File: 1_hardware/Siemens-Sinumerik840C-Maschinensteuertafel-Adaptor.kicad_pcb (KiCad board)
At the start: 2 copper layers, 235 x 118.7 mm, 33 parts, among them J111 SSW-132-24-L-D, J121 SSW-132-24-L-D, U1 STM32F103C8T6, U10 PCA9555PW,118, U11 PCA9555PW,118, U2 AP22652AW6-7, U3 LD1117S33CTR, U4 PCA9555PW,118, U5 PCA9555PW,118, U6 PCA9555PW,118, U7 PCA9555PW,118, U8 PCA9555PW,118, U9 PCA9555PW,118

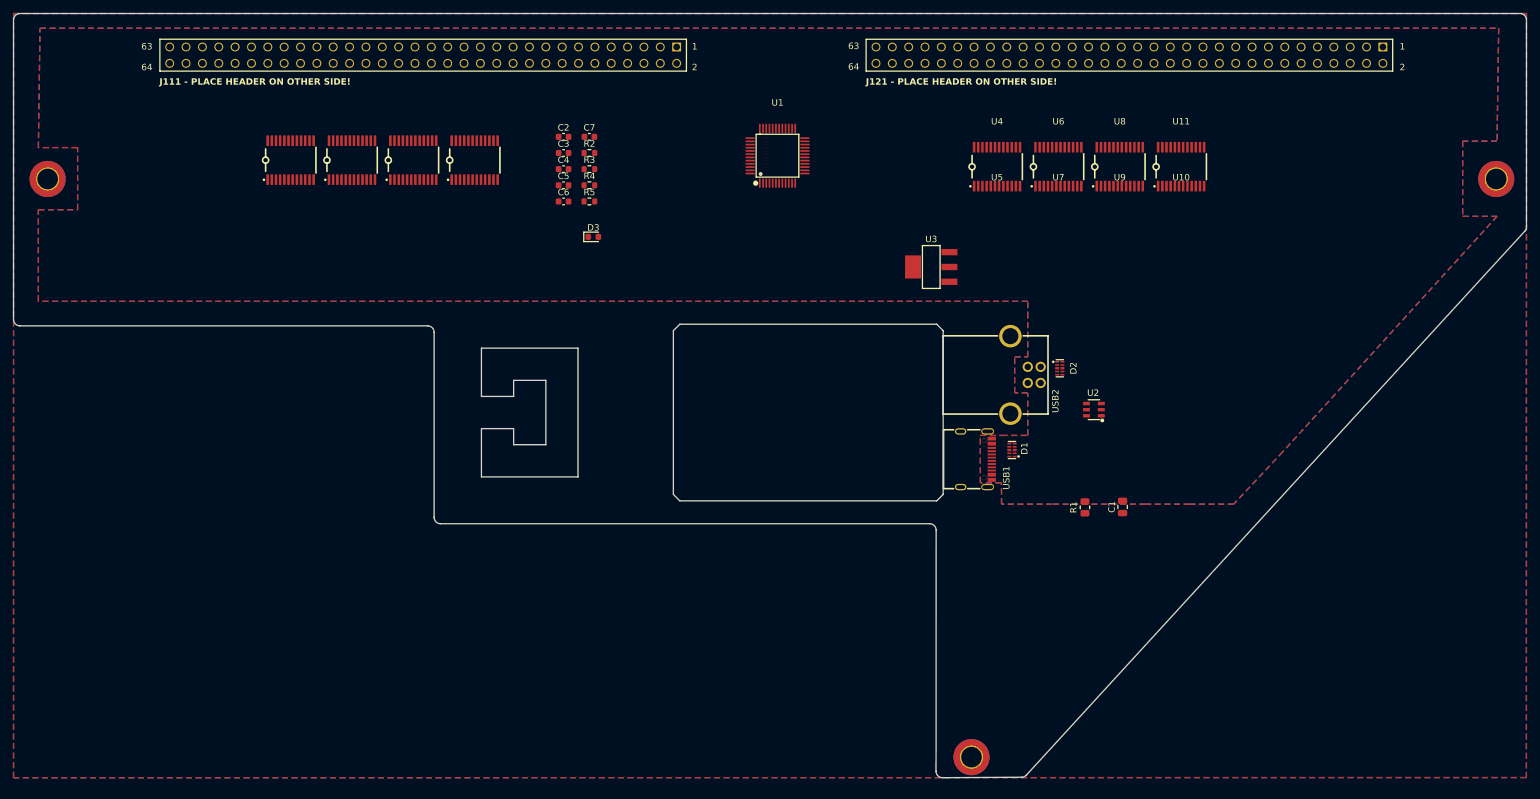
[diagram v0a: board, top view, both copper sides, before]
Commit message: finished most of schematic, init STM32 program
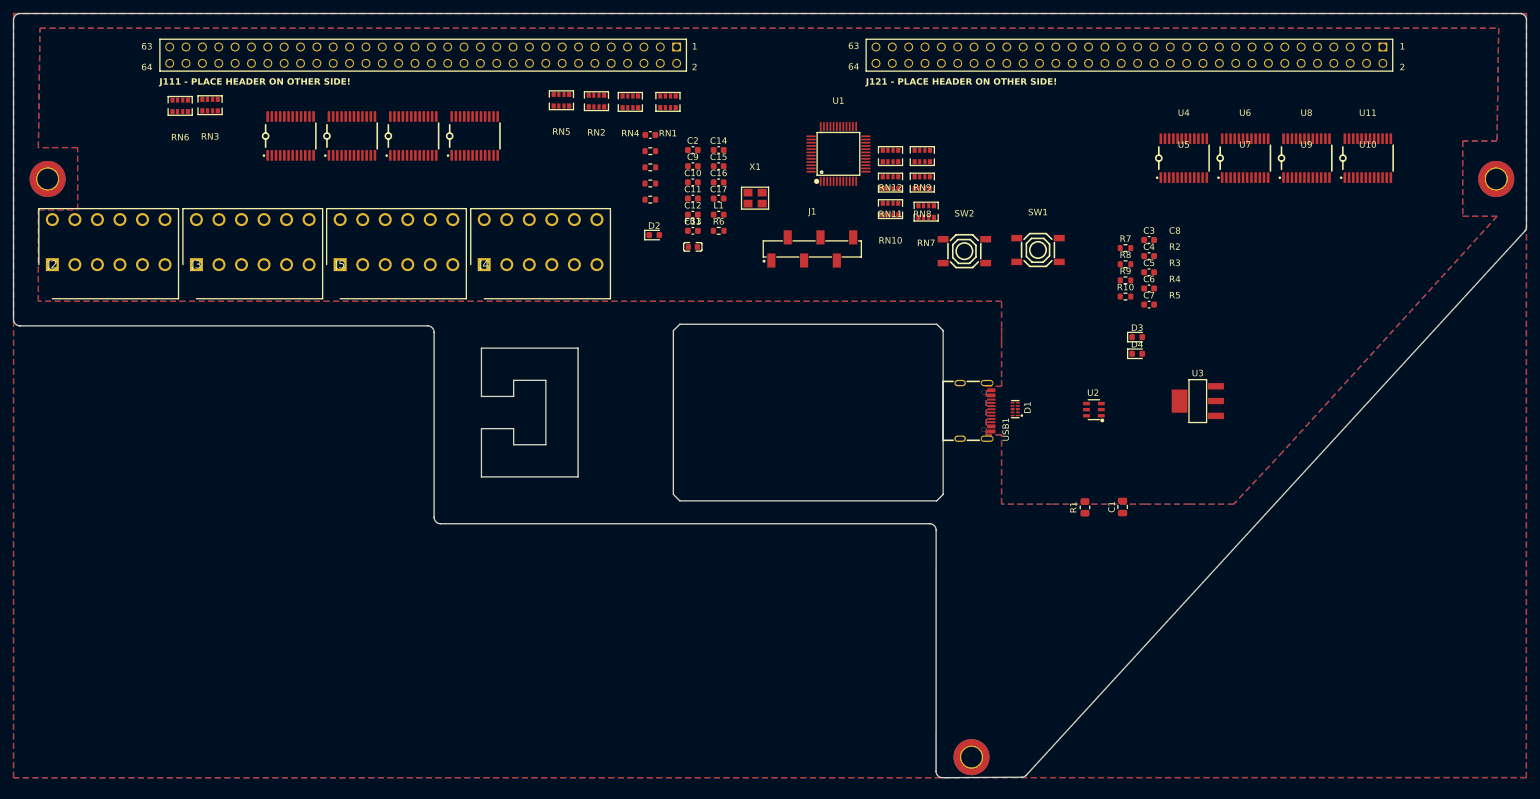
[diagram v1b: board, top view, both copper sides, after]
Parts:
- removed the D2 at (200.1, 80.6)
- removed USB2: USB-B10-BRW, easyeda2kicad:USB-B-TH_USB-B10-BRW
- added C10: 100n, Capacitor_SMD:C_0603_1608Metric, F.Cu at (143.1, 51.7)
- added C11: 100n, Capacitor_SMD:C_0603_1608Metric, F.Cu at (143.1, 54.2)
- added C12: 100n, Capacitor_SMD:C_0603_1608Metric, F.Cu at (143.1, 56.7)
- added C13: 100n, Capacitor_SMD:C_0603_1608Metric, F.Cu at (143.1, 59.2)
- added C14: 1u, Capacitor_SMD:C_0603_1608Metric, F.Cu at (147.1, 46.7)
- added C15: 100n, Capacitor_SMD:C_0603_1608Metric, F.Cu at (147.1, 49.2)
- added C16: 8p, Capacitor_SMD:C_0603_1608Metric, F.Cu at (147.1, 51.7)
- added C17: 8p, Capacitor_SMD:C_0603_1608Metric, F.Cu at (147.1, 54.2)
- added C2: 1u, Capacitor_SMD:C_0603_1608Metric, F.Cu at (143.1, 46.7)
- added C9: 4u7, Capacitor_SMD:C_0603_1608Metric, F.Cu at (143.1, 49.2)
- added D3: LED, LED_SMD:LED_0603_1608Metric, F.Cu at (212.1, 75.7)
- added D4: LED, LED_SMD:LED_0603_1608Metric, F.Cu at (212.1, 78.3)
- added FB1: 100R@100MHz, easyeda2kicad:L0603, F.Cu at (143.1, 61.7)
- added J1: ProgHeader, easyeda2kicad:HDR-SMD_6P-P2.54-V-M-LS4.8_R2, F.Cu at (161.7, 62.1)
- added J2: Power, CostumLibrary:1824460000 - LSF-SMT 3.500690 3.5SN BK TU, F.Cu at (43.6, 64.5)
- added J3: Buttons, CostumLibrary:1824460000 - LSF-SMT 3.500690 3.5SN BK TU, F.Cu at (66.0, 64.5)
- added J4: Reserve1, CostumLibrary:1824460000 - LSF-SMT 3.500690 3.5SN BK TU, F.Cu at (110.7, 64.5)
- added J5: Reserve2, CostumLibrary:1824460000 - LSF-SMT 3.500690 3.5SN BK TU, F.Cu at (88.3, 64.5)
- added L1: 27nH, Inductor_SMD:L_0603_1608Metric, F.Cu at (147.1, 56.7)
- added R10: 10k, Resistor_SMD:R_0603_1608Metric, F.Cu at (210.3, 69.4)
- added R6: 1k5, Resistor_SMD:R_0603_1608Metric, F.Cu at (147.1, 59.2)
- added R7: 10k, Resistor_SMD:R_0603_1608Metric, F.Cu at (210.3, 61.9)
- added R8: 1k5, Resistor_SMD:R_0603_1608Metric, F.Cu at (210.3, 64.4)
- added R9: 1k5, Resistor_SMD:R_0603_1608Metric, F.Cu at (210.3, 66.9)
- added RN1: 4x680R, easyeda2kicad:RES-ARRAY-SMD_0603-8P-L3.2-W1.6-BL, F.Cu at (139.2, 39.2)
- added RN10: 4x680R, easyeda2kicad:RES-ARRAY-SMD_0603-8P-L3.2-W1.6-BL, F.Cu at (173.8, 55.9)
- added RN11: 4x680R, easyeda2kicad:RES-ARRAY-SMD_0603-8P-L3.2-W1.6-BL, F.Cu at (173.8, 51.7)
- added RN12: 4x680R, easyeda2kicad:RES-ARRAY-SMD_0603-8P-L3.2-W1.6-BL, F.Cu at (173.8, 47.6)
- added RN2: 4x680R, easyeda2kicad:RES-ARRAY-SMD_0603-8P-L3.2-W1.6-BL, F.Cu at (128.1, 39.1)
- added RN3: 4x680R, easyeda2kicad:RES-ARRAY-SMD_0603-8P-L3.2-W1.6-BL, F.Cu at (68.1, 39.7)
- added RN4: 4x680R, easyeda2kicad:RES-ARRAY-SMD_0603-8P-L3.2-W1.6-BL, F.Cu at (133.4, 39.2)
- added RN5: 4x680R, easyeda2kicad:RES-ARRAY-SMD_0603-8P-L3.2-W1.6-BL, F.Cu at (122.7, 38.9)
- added RN6: 4x680R, easyeda2kicad:RES-ARRAY-SMD_0603-8P-L3.2-W1.6-BL, F.Cu at (63.5, 39.8)
- added RN7: 4x680R, easyeda2kicad:RES-ARRAY-SMD_0603-8P-L3.2-W1.6-BL, F.Cu at (179.3, 56.2)
- added RN8: 4x680R, easyeda2kicad:RES-ARRAY-SMD_0603-8P-L3.2-W1.6-BL, F.Cu at (178.8, 51.7)
- added RN9: 4x680R, easyeda2kicad:RES-ARRAY-SMD_0603-8P-L3.2-W1.6-BL, F.Cu at (178.8, 47.6)
- added SW1: TS-1187A-B-A-B, easyeda2kicad:SW-SMD_4P-L5.1-W5.1-P3.70-LS6.5-TL-2, F.Cu at (196.7, 62.2)
- added SW2: TS-1187A-B-A-B, easyeda2kicad:SW-SMD_4P-L5.1-W5.1-P3.70-LS6.5-TL-2, F.Cu at (185.3, 62.4)
- added X1: 16MHz, easyeda2kicad:CRYSTAL-SMD_4P-L3.2-W2.5-BL_SIT8008BI, F.Cu at (152.8, 54.2)
- C3: renamed from C2; value 0.1u -> 10u
- moved C3 92.3 mm to (214.0, 60.7)
- moved C4 92.3 mm to (214.0, 63.2)
- moved C5 92.3 mm to (214.0, 65.7)
- moved C6 92.3 mm to (214.0, 68.2)
- moved C7 92.3 mm to (214.0, 70.7)
- moved U3 46.3 mm to (221.5, 85.7)
- moved U11 29.0 mm to (248.0, 47.9)
- moved U4 29.0 mm to (219.4, 47.9)
- moved U6 29.0 mm to (228.9, 47.9)
- moved U8 29.0 mm to (238.4, 47.9)
- moved D2 9.47 mm to (137.1, 59.9)
- moved U1 9.47 mm to (165.7, 47.3)
- moved C8 9.47 mm to (136.5, 44.4)
- moved R2 9.47 mm to (136.5, 46.9)
- moved R3 9.47 mm to (136.5, 49.4)
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- renumbered C3 to C4, C4 to C5, C5 to C6, C6 to C7, C7 to C8, D3 to D2
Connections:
- C3 pad 2: USB_VBUS -> Net-(U2-IN)
- C4 pad 2: USB_VBUS -> Net-(U2-IN)
- J111 pad 01: LED-C15 -> Net-(J111-Pad01)
- J111 pad 02: LED-C06 -> Net-(J111-Pad02)
- J111 pad 03: LED-C08 -> Net-(J111-Pad03)
- J111 pad 04: LED-C09 -> Net-(J111-Pad04)
- J111 pad 05: LED-C11 -> Net-(J111-Pad05)
- J111 pad 06: LED-C12 -> Net-(J111-Pad06)
- J111 pad 07: LED-C05 -> Net-(J111-Pad07)
- J111 pad 08: LED-C03 -> Net-(J111-Pad08)
- J111 pad 09: LED-C02 -> Net-(J111-Pad09)
- J111 pad 10: LED-B15 -> Net-(J111-Pad10)
- J111 pad 11: LED-B14 -> Net-(J111-Pad11)
- J111 pad 12: LED-B13 -> Net-(J111-Pad12)
- J111 pad 13: LED-B12 -> Net-(J111-Pad13)
- J111 pad 14: LED-B11 -> Net-(J111-Pad14)
- J111 pad 15: LED-B10 -> Net-(J111-Pad15)
- J111 pad 16: LED-B09 -> Net-(J111-Pad16)
- J111 pad 17: /Headers/GND -> GND
- J111 pad 27: /Headers/GND -> GND
- J111 pad 34: /Headers/VCC -> +3V3
- J111 pad 45: /Headers/GND -> GND
- J111 pad 52: /Headers/VCC -> +3V3
- J111 pad 55: /Headers/GND -> GND
- J111 pad 56: LED-B08 -> Net-(J111-Pad56)
- J111 pad 57: LED-B07 -> Net-(J111-Pad57)
- J111 pad 58: LED-B06 -> Net-(J111-Pad58)
- J111 pad 59: LED-B05 -> Net-(J111-Pad59)
- J111 pad 60: LED-B04 -> Net-(J111-Pad60)
- J111 pad 61: LED-B03 -> Net-(J111-Pad61)
- J111 pad 62: LED-B02 -> Net-(J111-Pad62)
- J111 pad 63: LED-B01 -> Net-(J111-Pad63)
- J121 pad 01: LED-A10 -> Net-(J121-Pad01)
- J121 pad 02: LED-A07 -> Net-(J121-Pad02)
- J121 pad 03: LED-A04 -> Net-(J121-Pad03)
- J121 pad 04: LED-A01 -> Net-(J121-Pad04)
- J121 pad 05: LED-A06 -> Net-(J121-Pad05)
- J121 pad 06: LED-A08 -> Net-(J121-Pad06)
- J121 pad 07: LED-A09 -> Net-(J121-Pad07)
- J121 pad 08: LED-A11 -> Net-(J121-Pad08)
- J121 pad 09: LED-A12 -> Net-(J121-Pad09)
- J121 pad 10: LED-A05 -> Net-(J121-Pad10)
- J121 pad 11: LED-A03 -> Net-(J121-Pad11)
- J121 pad 12: LED-A02 -> Net-(J121-Pad12)
- J121 pad 13: LED-A15 -> Net-(J121-Pad13)
- J121 pad 14: LED-A16 -> Net-(J121-Pad14)
- J121 pad 15: LED-E01 -> Net-(J121-Pad15)
- J121 pad 16: LED-E02 -> Net-(J121-Pad16)
- J121 pad 17: /Headers/GND -> GND
- J121 pad 27: /Headers/GND -> GND
- J121 pad 34: /Headers/VCC -> +3V3
- J121 pad 45: /Headers/GND -> GND
- J121 pad 52: /Headers/VCC -> +3V3
- J121 pad 55: /Headers/GND -> GND
- J121 pad 56: LED-D01 -> Net-(J121-Pad56)
- J121 pad 57: LED-D02 -> Net-(J121-Pad57)
- J121 pad 58: LED-A14 -> Net-(J121-Pad58)
- J121 pad 59: LED-C10 -> Net-(J121-Pad59)
- J121 pad 60: LED-C07 -> Net-(J121-Pad60)
- J121 pad 61: LED-C04 -> Net-(J121-Pad61)
- J121 pad 62: LED-C01 -> Net-(J121-Pad62)
- J121 pad 63: LED-C13 -> Net-(J121-Pad63)
- R5 pad 1: USB_VBUS -> Net-(U2-IN)
- U1 pad 1: unconnected-(U1-VBAT-Pad1) -> +3V3
- U1 pad 11: unconnected-(U1-PA1-Pad11) -> DebugLED
- U1 pad 12: unconnected-(U1-PA2-Pad12) -> Button-A15
- U1 pad 13: unconnected-(U1-PA3-Pad13) -> Button-D01
- U1 pad 14: unconnected-(U1-PA4-Pad14) -> Button-E01
- U1 pad 15: unconnected-(U1-PA5-Pad15) -> uC_IO1
- U1 pad 16: unconnected-(U1-PA6-Pad16) -> uC_IO2
- U1 pad 17: unconnected-(U1-PA7-Pad17) -> uC_IO3
- U1 pad 18: unconnected-(U1-PB0-Pad18) -> uC_IO4
- U1 pad 19: unconnected-(U1-PB1-Pad19) -> uC_IO5
- U1 pad 20: unconnected-(U1-PB2-Pad20) -> uC_IO6
- U1 pad 21: unconnected-(U1-PB10-Pad21) -> I2C2_SCL
- U1 pad 22: unconnected-(U1-PB11-Pad22) -> I2C2_SDA
- U1 pad 23: unconnected-(U1-VSS_1-Pad23) -> GND
- U1 pad 24: unconnected-(U1-VDD_1-Pad24) -> +3V3
- U1 pad 29: unconnected-(U1-PA8-Pad29) -> AIN1
- U1 pad 30: unconnected-(U1-PA9-Pad30) -> AIN2
- U1 pad 32: unconnected-(U1-PA11-Pad32) -> USB_D-
- U1 pad 33: unconnected-(U1-PA12-Pad33) -> USB_D+
- U1 pad 34: unconnected-(U1-PA13-Pad34) -> SWDIO
- U1 pad 35: unconnected-(U1-VSS_2-Pad35) -> GND
- U1 pad 36: unconnected-(U1-VDD_2-Pad36) -> +3V3
- U1 pad 37: unconnected-(U1-PA14-Pad37) -> SWCLK
- U1 pad 42: unconnected-(U1-PB6-Pad42) -> I2C1_SCL
- U1 pad 43: unconnected-(U1-PB7-Pad43) -> I2C1_SDA
- U1 pad 44: unconnected-(U1-BOOT0-Pad44) -> BOOT0
- U1 pad 47: unconnected-(U1-VSS_3-Pad47) -> GND
- U1 pad 48: unconnected-(U1-VDD_3-Pad48) -> +3V3
- U1 pad 5: unconnected-(U1-PD0-OSC_IN-Pad5) -> HSE_IN
- U1 pad 6: unconnected-(U1-PD1-OSC_OUT-Pad6) -> HSE_OUT
- U1 pad 7: unconnected-(U1-NRST-Pad7) -> RST
- U1 pad 8: unconnected-(U1-VSSA-Pad8) -> GND
- U1 pad 9: unconnected-(U1-VDDA-Pad9) -> +3V3A
- U10 pad 22: /Inputs Outputs on Extenders/I2C_Bus2_SCL -> I2C2_SCL
- U10 pad 23: /Inputs Outputs on Extenders/I2C_Bus2_SDA -> I2C2_SDA
- U11 pad 22: /Inputs Outputs on Extenders/I2C_Bus2_SCL -> I2C2_SCL
- U11 pad 23: /Inputs Outputs on Extenders/I2C_Bus2_SDA -> I2C2_SDA
- U2 pad 1: USB_VBUS -> Net-(U2-IN)
- U4 pad 22: /Inputs Outputs on Extenders/I2C_Bus1_SCL -> I2C1_SCL
- U4 pad 23: /Inputs Outputs on Extenders/I2C_Bus1_SDA -> I2C1_SDA
- U5 pad 22: /Inputs Outputs on Extenders/I2C_Bus1_SCL -> I2C1_SCL
- U5 pad 23: /Inputs Outputs on Extenders/I2C_Bus1_SDA -> I2C1_SDA
- U6 pad 22: /Inputs Outputs on Extenders/I2C_Bus1_SCL -> I2C1_SCL
- U6 pad 23: /Inputs Outputs on Extenders/I2C_Bus1_SDA -> I2C1_SDA
- U7 pad 22: /Inputs Outputs on Extenders/I2C_Bus1_SCL -> I2C1_SCL
- U7 pad 23: /Inputs Outputs on Extenders/I2C_Bus1_SDA -> I2C1_SDA
- U8 pad 22: /Inputs Outputs on Extenders/I2C_Bus2_SCL -> I2C2_SCL
- U8 pad 23: /Inputs Outputs on Extenders/I2C_Bus2_SDA -> I2C2_SDA
- U9 pad 22: /Inputs Outputs on Extenders/I2C_Bus2_SCL -> I2C2_SCL
- U9 pad 23: /Inputs Outputs on Extenders/I2C_Bus2_SDA -> I2C2_SDA

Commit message: finished schematics and board
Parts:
- removed the J4 at (110.7, 64.5)
- added R11: 10k, Resistor_SMD:R_0603_1608Metric, F.Cu at (142.5, 47.1)
- added R12: 10k, Resistor_SMD:R_0603_1608Metric, F.Cu at (122.2, 47.1)
- added R13: 10k, Resistor_SMD:R_0603_1608Metric, F.Cu at (96.8, 43.3)
- added R14: 10k, Resistor_SMD:R_0603_1608Metric, F.Cu at (73.7, 47.1)
- added R15: 10k, Resistor_SMD:R_0603_1608Metric, F.Cu at (252.5, 47.1)
- added R16: 10k, Resistor_SMD:R_0603_1608Metric, F.Cu at (232.0, 47.1)
- added R17: 10k, Resistor_SMD:R_0603_1608Metric, F.Cu at (206.6, 47.1)
- added R18: 10k, Resistor_SMD:R_0603_1608Metric, F.Cu at (183.7, 47.1)
- added R19: 1k5, Resistor_SMD:R_0603_1608Metric, F.Cu at (227.6, 88.0)
- added R20: 1k5, Resistor_SMD:R_0603_1608Metric, F.Cu at (225.9, 88.0)
- added R21: 1k5, Resistor_SMD:R_0603_1608Metric, F.Cu at (226.4, 66.6)
- added R22: 1k5, Resistor_SMD:R_0603_1608Metric, F.Cu at (228.1, 66.6)
- C1: footprint Capacitor_SMD:C_0805_2012Metric -> Capacitor_SMD:C_1206_3216Metric
- H1, H2, H3: footprint MountingHole:MountingHole_3.2mm_M3_DIN965_Pad_TopBottom -> MountingHole:MountingHole_3.2mm_M3_DIN965_Pad
- R1: footprint Resistor_SMD:R_0805_2012Metric -> Resistor_SMD:R_1206_3216Metric
- moved U6 137.7 mm to (91.2, 43.3), turned to 180 degrees
- moved U9 126.7 mm to (226.4, 47.1), turned to 180 degrees
- moved C9 98.2 mm to (238.6, 72.5)
- moved C10 97.2 mm to (234.5, 84.9), turned to 180 degrees
- moved C17 95.7 mm to (237.8, 84.9), turned to 180 degrees
- moved C16 95.3 mm to (238.6, 78.6)
- moved C14 93.9 mm to (236.0, 77.0), turned to -90 degrees
- moved L1 93.3 mm to (238.6, 75.5), turned to 180 degrees
- moved U10 91.8 mm to (201.0, 47.1), turned to 180 degrees
- moved C13 91.7 mm to (231.2, 84.9)
- moved C15 91.7 mm to (234.5, 77.0), turned to -90 degrees
- moved X1 89.1 mm to (237.5, 81.6), turned to 180 degrees
- moved U4 82.4 mm to (137.0, 47.1), turned to 180 degrees
- moved C11 81.6 mm to (222.8, 71.7)
- moved C12 81.5 mm to (220.8, 81.4), turned to -90 degrees
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- renumbered J5 to J4
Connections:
- C1 pad 1: CGND -> GND
- C1 pad 2: GND -> CGND
- D1 pad 10: unconnected-(D1-NC-Pad10) -> USB_D+
- D1 pad 7: unconnected-(D1-NC-Pad7) -> USB_VBUS
- D1 pad 9: unconnected-(D1-NC-Pad9) -> USB_D-
- H1 pad 1: (no net) -> CGND
- H2 pad 1: (no net) -> CGND
- H3 pad 1: (no net) -> CGND
- J111 pad 01: Net-(J111-Pad01) -> P1.01
- J111 pad 02: Net-(J111-Pad02) -> P1.02
- J111 pad 03: Net-(J111-Pad03) -> P1.03
- J111 pad 04: Net-(J111-Pad04) -> P1.04
- J111 pad 05: Net-(J111-Pad05) -> P1.05
- J111 pad 06: Net-(J111-Pad06) -> P1.06
- J111 pad 07: Net-(J111-Pad07) -> P1.07
- J111 pad 08: Net-(J111-Pad08) -> P1.08
- J111 pad 09: Net-(J111-Pad09) -> P1.09
- J111 pad 10: Net-(J111-Pad10) -> P1.10
- J111 pad 11: Net-(J111-Pad11) -> P1.11
- J111 pad 12: Net-(J111-Pad12) -> P1.12
- J111 pad 13: Net-(J111-Pad13) -> P1.13
- J111 pad 14: Net-(J111-Pad14) -> P1.14
- J111 pad 15: Net-(J111-Pad15) -> P1.15
- J111 pad 16: Net-(J111-Pad16) -> P1.16
- J111 pad 34: +3V3 -> VCC
- J111 pad 52: +3V3 -> VCC
- J111 pad 56: Net-(J111-Pad56) -> P1.56
- J111 pad 57: Net-(J111-Pad57) -> P1.57
- J111 pad 58: Net-(J111-Pad58) -> P1.58
- J111 pad 59: Net-(J111-Pad59) -> P1.59
- J111 pad 60: Net-(J111-Pad60) -> P1.60
- J111 pad 61: Net-(J111-Pad61) -> P1.61
- J111 pad 62: Net-(J111-Pad62) -> P1.62
- J111 pad 63: Net-(J111-Pad63) -> P1.63
- J121 pad 01: Net-(J121-Pad01) -> P2.01
- J121 pad 02: Net-(J121-Pad02) -> P2.02
- J121 pad 03: Net-(J121-Pad03) -> P2.03
- J121 pad 04: Net-(J121-Pad04) -> P2.04
- J121 pad 05: Net-(J121-Pad05) -> P2.05
- J121 pad 06: Net-(J121-Pad06) -> P2.06
- J121 pad 07: Net-(J121-Pad07) -> P2.07
- J121 pad 08: Net-(J121-Pad08) -> P2.08
- J121 pad 09: Net-(J121-Pad09) -> P2.09
- J121 pad 10: Net-(J121-Pad10) -> P2.10
- J121 pad 11: Net-(J121-Pad11) -> P2.11
- J121 pad 12: Net-(J121-Pad12) -> P2.12
- J121 pad 13: Net-(J121-Pad13) -> P2.13
- J121 pad 14: Net-(J121-Pad14) -> P2.14
- J121 pad 15: Net-(J121-Pad15) -> P2.15
- J121 pad 16: Net-(J121-Pad16) -> P2.16
- J121 pad 34: +3V3 -> VCC
- J121 pad 52: +3V3 -> VCC
- J121 pad 56: Net-(J121-Pad56) -> P2.56
- J121 pad 57: Net-(J121-Pad57) -> P2.57
- J121 pad 58: Net-(J121-Pad58) -> P2.58
- J121 pad 59: Net-(J121-Pad59) -> P2.59
- J121 pad 60: Net-(J121-Pad60) -> P2.60
- J121 pad 61: Net-(J121-Pad61) -> P2.61
- J121 pad 62: Net-(J121-Pad62) -> P2.62
- J121 pad 63: Net-(J121-Pad63) -> P2.63
- J2 pad 5: +3V3 -> VCC
- J2 pad 6: +3V3 -> VCC
- J2 pad 7: +3V3 -> VCC
- J2 pad 8: +3V3 -> VCC
- RN1 pad 1: LED-C15 -> P1.01
- RN1 pad 2: LED-C08 -> P1.02
- RN1 pad 3: LED-C11 -> P1.03
- RN1 pad 4: LED-C05 -> P1.04
- RN1 pad 5: Net-(J111-Pad07) -> LED-C09
- RN1 pad 6: Net-(J111-Pad05) -> LED-C08
- RN1 pad 7: Net-(J111-Pad03) -> LED-C06
- RN1 pad 8: Net-(J111-Pad01) -> LED-C15
- RN10 pad 1: LED-A07 -> P2.13
- RN10 pad 2: LED-A01 -> P2.14
- RN10 pad 3: LED-A08 -> P2.15
- RN10 pad 4: LED-A11 -> P2.16
- RN10 pad 5: Net-(J121-Pad08) -> LED-E02
- RN10 pad 6: Net-(J121-Pad06) -> LED-E01
- RN10 pad 7: Net-(J121-Pad04) -> LED-A16
- RN10 pad 8: Net-(J121-Pad02) -> LED-A15
- RN11 pad 1: LED-A05 -> P2.56
- RN11 pad 2: LED-A02 -> P2.57
- RN11 pad 3: LED-A16 -> P2.58
- RN11 pad 4: LED-E02 -> P2.59
- RN11 pad 5: Net-(J121-Pad16) -> LED-C10
- RN11 pad 6: Net-(J121-Pad14) -> LED-A14
- RN11 pad 7: Net-(J121-Pad12) -> LED-D02
- RN11 pad 8: Net-(J121-Pad10) -> LED-D01
- RN12 pad 1: LED-D01 -> P2.60
- RN12 pad 2: LED-A14 -> P2.61
- RN12 pad 3: LED-C07 -> P2.62
- RN12 pad 4: LED-C01 -> P2.63
- RN12 pad 5: Net-(J121-Pad62) -> LED-C13
- RN12 pad 6: Net-(J121-Pad60) -> LED-C01
- RN12 pad 7: Net-(J121-Pad58) -> LED-C04
- RN12 pad 8: Net-(J121-Pad56) -> LED-C07
- RN2 pad 1: LED-C02 -> P1.05
- RN2 pad 2: LED-B14 -> P1.06
- RN2 pad 3: LED-B12 -> P1.07
- RN2 pad 4: LED-B10 -> P1.08
- RN2 pad 5: Net-(J111-Pad15) -> LED-C03
- RN2 pad 6: Net-(J111-Pad13) -> LED-C05
- RN2 pad 7: Net-(J111-Pad11) -> LED-C12
- RN2 pad 8: Net-(J111-Pad09) -> LED-C11
- RN3 pad 1: LED-B07 -> P1.09
- RN3 pad 2: LED-B05 -> P1.10
- RN3 pad 3: LED-B03 -> P1.11
- RN3 pad 4: LED-B01 -> P1.12
- RN3 pad 5: Net-(J111-Pad63) -> LED-B13
- RN3 pad 6: Net-(J111-Pad61) -> LED-B14
- RN3 pad 7: Net-(J111-Pad59) -> LED-B15
- RN3 pad 8: Net-(J111-Pad57) -> LED-C02
- RN4 pad 1: LED-C06 -> P1.13
- RN4 pad 2: LED-C09 -> P1.14
- RN4 pad 3: LED-C12 -> P1.15
- RN4 pad 4: LED-C03 -> P1.16
- RN4 pad 5: Net-(J111-Pad08) -> LED-B09
- RN4 pad 6: Net-(J111-Pad06) -> LED-B10
- RN4 pad 7: Net-(J111-Pad04) -> LED-B11
- RN4 pad 8: Net-(J111-Pad02) -> LED-B12
- RN5 pad 1: LED-B15 -> P1.56
- RN5 pad 2: LED-B13 -> P1.57
- RN5 pad 3: LED-B11 -> P1.58
- RN5 pad 4: LED-B09 -> P1.59
- RN5 pad 5: Net-(J111-Pad16) -> LED-B05
- RN5 pad 6: Net-(J111-Pad14) -> LED-B06
- RN5 pad 7: Net-(J111-Pad12) -> LED-B07
- RN5 pad 8: Net-(J111-Pad10) -> LED-B08
- RN6 pad 1: LED-B08 -> P1.60
- RN6 pad 2: LED-B06 -> P1.61
- RN6 pad 3: LED-B04 -> P1.62
- RN6 pad 4: LED-B02 -> P1.63
- RN6 pad 5: Net-(J111-Pad62) -> LED-B01
- RN6 pad 6: Net-(J111-Pad60) -> LED-B02
- RN6 pad 7: Net-(J111-Pad58) -> LED-B03
- RN6 pad 8: Net-(J111-Pad56) -> LED-B04
- RN7 pad 1: LED-A10 -> P2.01
- RN7 pad 2: LED-A04 -> P2.02
- RN7 pad 3: LED-A06 -> P2.03
- RN7 pad 4: LED-A09 -> P2.04
- RN7 pad 5: Net-(J121-Pad07) -> LED-A01
- RN7 pad 6: Net-(J121-Pad05) -> LED-A04
- RN7 pad 7: Net-(J121-Pad03) -> LED-A07
- RN7 pad 8: Net-(J121-Pad01) -> LED-A10
- RN8 pad 1: LED-A12 -> P2.05
- RN8 pad 2: LED-A03 -> P2.06
- RN8 pad 3: LED-A15 -> P2.07
- RN8 pad 4: LED-E01 -> P2.08
- RN8 pad 5: Net-(J121-Pad15) -> LED-A11
- RN8 pad 6: Net-(J121-Pad13) -> LED-A09
- RN8 pad 7: Net-(J121-Pad11) -> LED-A08
- RN8 pad 8: Net-(J121-Pad09) -> LED-A06
- RN9 pad 1: LED-D02 -> P2.09
- RN9 pad 2: LED-C10 -> P2.10
- RN9 pad 3: LED-C04 -> P2.11
- RN9 pad 4: LED-C13 -> P2.12
- RN9 pad 5: Net-(J121-Pad63) -> LED-A02
- RN9 pad 6: Net-(J121-Pad61) -> LED-A03
- RN9 pad 7: Net-(J121-Pad59) -> LED-A05
- RN9 pad 8: Net-(J121-Pad57) -> LED-A12
- U1 pad 12: Button-A15 -> Button-~{A15}
- U1 pad 13: Button-D01 -> Button-~{D01}
- U1 pad 14: Button-E01 -> Button-~{E01}
- U1 pad 15: uC_IO1 -> unconnected-(U1-PA5-Pad15)
- U1 pad 16: uC_IO2 -> unconnected-(U1-PA6-Pad16)
- U1 pad 17: uC_IO3 -> unconnected-(U1-PA7-Pad17)
- U1 pad 18: uC_IO4 -> EXP_INT1
- U1 pad 19: uC_IO5 -> EXP_INT2
- U1 pad 20: uC_IO6 -> EXP_INT3
- U1 pad 39: unconnected-(U1-PB3-Pad39) -> EXP_INT4
- U1 pad 40: unconnected-(U1-PB4-Pad40) -> EXP_INT5
- U1 pad 41: unconnected-(U1-PB5-Pad41) -> EXP_INT6
- U1 pad 45: unconnected-(U1-PB8-Pad45) -> EXP_INT7
- U1 pad 46: unconnected-(U1-PB9-Pad46) -> EXP_INT8
- U10 pad 1: unconnected-(U10-~{INT}-Pad1) -> EXP_INT7
- U10 pad 10: unconnected-(U10-IO0_6-Pad10) -> Button-D02
- U10 pad 11: unconnected-(U10-IO0_7-Pad11) -> ENC1-X14
- U10 pad 12: unconnected-(U10-VSS-Pad12) -> GND
- U10 pad 13: unconnected-(U10-IO1_0-Pad13) -> Schluessel2
- U10 pad 14: unconnected-(U10-IO1_1-Pad14) -> Button-A14
- U10 pad 15: unconnected-(U10-IO1_2-Pad15) -> Schluessel0
- U10 pad 16: unconnected-(U10-IO1_3-Pad16) -> Schluessel3
- U10 pad 17: unconnected-(U10-IO1_4-Pad17) -> Button-A13
- U10 pad 2: unconnected-(U10-A1-Pad2) -> +3V3
- U10 pad 21: unconnected-(U10-A0-Pad21) -> GND
- U10 pad 24: unconnected-(U10-VDD-Pad24) -> +3V3
- U10 pad 3: unconnected-(U10-A2-Pad3) -> GND
- U10 pad 4: unconnected-(U10-IO0_0-Pad4) -> ENC1-X11
- U10 pad 5: unconnected-(U10-IO0_1-Pad5) -> Button-A16
- U10 pad 6: unconnected-(U10-IO0_2-Pad6) -> ENC1-X12
- U10 pad 7: unconnected-(U10-IO0_3-Pad7) -> ENC1-X15
- U10 pad 8: unconnected-(U10-IO0_4-Pad8) -> Button-E02
- U10 pad 9: unconnected-(U10-IO0_5-Pad9) -> ENC1-X13
- U11 pad 1: unconnected-(U11-~{INT}-Pad1) -> EXP_INT8
- U11 pad 10: unconnected-(U11-IO0_6-Pad10) -> LED-C01
- U11 pad 11: unconnected-(U11-IO0_7-Pad11) -> LED-C13
- U11 pad 12: unconnected-(U11-VSS-Pad12) -> GND
- U11 pad 2: unconnected-(U11-A1-Pad2) -> +3V3
- U11 pad 21: unconnected-(U11-A0-Pad21) -> +3V3
- U11 pad 24: unconnected-(U11-VDD-Pad24) -> +3V3
- U11 pad 3: unconnected-(U11-A2-Pad3) -> GND
- U11 pad 4: unconnected-(U11-IO0_0-Pad4) -> LED-D01
- U11 pad 5: unconnected-(U11-IO0_1-Pad5) -> LED-D02
- U11 pad 6: unconnected-(U11-IO0_2-Pad6) -> LED-A14
- U11 pad 7: unconnected-(U11-IO0_3-Pad7) -> LED-C10
- U11 pad 8: unconnected-(U11-IO0_4-Pad8) -> LED-C07
- U11 pad 9: unconnected-(U11-IO0_5-Pad9) -> LED-C04
- U4 pad 1: unconnected-(U4-~{INT}-Pad1) -> EXP_INT1
- U4 pad 10: unconnected-(U4-IO0_6-Pad10) -> LED-C05
- U4 pad 11: unconnected-(U4-IO0_7-Pad11) -> LED-C03
- U4 pad 12: unconnected-(U4-VSS-Pad12) -> GND
- U4 pad 13: unconnected-(U4-IO1_0-Pad13) -> LED-C02
- U4 pad 14: unconnected-(U4-IO1_1-Pad14) -> LED-B15
- U4 pad 15: unconnected-(U4-IO1_2-Pad15) -> LED-B14
- U4 pad 16: unconnected-(U4-IO1_3-Pad16) -> LED-B13
- U4 pad 17: unconnected-(U4-IO1_4-Pad17) -> LED-B12
- U4 pad 18: unconnected-(U4-IO1_5-Pad18) -> LED-B11
- U4 pad 19: unconnected-(U4-IO1_6-Pad19) -> LED-B10
- U4 pad 2: unconnected-(U4-A1-Pad2) -> GND
- U4 pad 20: unconnected-(U4-IO1_7-Pad20) -> LED-B09
- U4 pad 21: unconnected-(U4-A0-Pad21) -> GND
- U4 pad 24: unconnected-(U4-VDD-Pad24) -> +3V3
- U4 pad 3: unconnected-(U4-A2-Pad3) -> +3V3
- U4 pad 4: unconnected-(U4-IO0_0-Pad4) -> LED-C15
- U4 pad 5: unconnected-(U4-IO0_1-Pad5) -> LED-C06
- U4 pad 6: unconnected-(U4-IO0_2-Pad6) -> LED-C08
- U4 pad 7: unconnected-(U4-IO0_3-Pad7) -> LED-C09
- U4 pad 8: unconnected-(U4-IO0_4-Pad8) -> LED-C11
- U4 pad 9: unconnected-(U4-IO0_5-Pad9) -> LED-C12
- U5 pad 1: unconnected-(U5-~{INT}-Pad1) -> EXP_INT2
- U5 pad 10: unconnected-(U5-IO0_6-Pad10) -> Button-C01
- U5 pad 11: unconnected-(U5-IO0_7-Pad11) -> Button-C11
- U5 pad 12: unconnected-(U5-VSS-Pad12) -> GND
- U5 pad 13: unconnected-(U5-IO1_0-Pad13) -> Schluessel1
- U5 pad 14: unconnected-(U5-IO1_1-Pad14) -> Button-C14
- U5 pad 15: unconnected-(U5-IO1_2-Pad15) -> Button-C12
- U5 pad 16: unconnected-(U5-IO1_3-Pad16) -> Button-C13
- U5 pad 17: unconnected-(U5-IO1_4-Pad17) -> Button-C05
- U5 pad 18: unconnected-(U5-IO1_5-Pad18) -> Button-C15
- U5 pad 19: unconnected-(U5-IO1_6-Pad19) -> Button-C03
- U5 pad 2: unconnected-(U5-A1-Pad2) -> GND
- U5 pad 20: unconnected-(U5-IO1_7-Pad20) -> Button-C02
- U5 pad 21: unconnected-(U5-A0-Pad21) -> +3V3
- U5 pad 24: unconnected-(U5-VDD-Pad24) -> +3V3
- U5 pad 3: unconnected-(U5-A2-Pad3) -> +3V3
- U5 pad 4: unconnected-(U5-IO0_0-Pad4) -> Button-C10
- U5 pad 5: unconnected-(U5-IO0_1-Pad5) -> Button-C06
- U5 pad 6: unconnected-(U5-IO0_2-Pad6) -> Button-C07
- U5 pad 7: unconnected-(U5-IO0_3-Pad7) -> Button-C08
- U5 pad 8: unconnected-(U5-IO0_4-Pad8) -> Button-C04
- U5 pad 9: unconnected-(U5-IO0_5-Pad9) -> Button-C09
- U6 pad 1: unconnected-(U6-~{INT}-Pad1) -> EXP_INT3
- U6 pad 10: unconnected-(U6-IO0_6-Pad10) -> Button-B05
- U6 pad 11: unconnected-(U6-IO0_7-Pad11) -> Button-B12
- U6 pad 12: unconnected-(U6-VSS-Pad12) -> GND
- U6 pad 13: unconnected-(U6-IO1_0-Pad13) -> Button-B11
- U6 pad 14: unconnected-(U6-IO1_1-Pad14) -> Button-B04
- U6 pad 15: unconnected-(U6-IO1_2-Pad15) -> Button-B10
- U6 pad 16: unconnected-(U6-IO1_3-Pad16) -> Button-B03
- U6 pad 17: unconnected-(U6-IO1_4-Pad17) -> Button-B09
- U6 pad 18: unconnected-(U6-IO1_5-Pad18) -> Button-B02
- U6 pad 19: unconnected-(U6-IO1_6-Pad19) -> Button-B01
- U6 pad 2: unconnected-(U6-A1-Pad2) -> +3V3
- U6 pad 21: unconnected-(U6-A0-Pad21) -> GND
- U6 pad 24: unconnected-(U6-VDD-Pad24) -> +3V3
- U6 pad 3: unconnected-(U6-A2-Pad3) -> +3V3
- U6 pad 4: unconnected-(U6-IO0_0-Pad4) -> Button-B08
- U6 pad 5: unconnected-(U6-IO0_1-Pad5) -> Button-B15
- U6 pad 6: unconnected-(U6-IO0_2-Pad6) -> Button-B07
- U6 pad 7: unconnected-(U6-IO0_3-Pad7) -> Button-B14
- U6 pad 8: unconnected-(U6-IO0_4-Pad8) -> Button-B06
- U6 pad 9: unconnected-(U6-IO0_5-Pad9) -> Button-B13
- U7 pad 1: unconnected-(U7-~{INT}-Pad1) -> EXP_INT4
- U7 pad 10: unconnected-(U7-IO0_6-Pad10) -> LED-B02
- U7 pad 11: unconnected-(U7-IO0_7-Pad11) -> LED-B01
- U7 pad 12: unconnected-(U7-VSS-Pad12) -> GND
- U7 pad 13: unconnected-(U7-IO1_0-Pad13) -> Input-Res01
- U7 pad 14: unconnected-(U7-IO1_1-Pad14) -> Input-Res02
- U7 pad 15: unconnected-(U7-IO1_2-Pad15) -> Input-Res03
- U7 pad 16: unconnected-(U7-IO1_3-Pad16) -> Input-Res04
- U7 pad 17: unconnected-(U7-IO1_4-Pad17) -> Output-Res01
- U7 pad 18: unconnected-(U7-IO1_5-Pad18) -> Output-Res02
- U7 pad 19: unconnected-(U7-IO1_6-Pad19) -> Output-Res03
- U7 pad 2: unconnected-(U7-A1-Pad2) -> +3V3
- U7 pad 20: unconnected-(U7-IO1_7-Pad20) -> Output-Res04
- U7 pad 21: unconnected-(U7-A0-Pad21) -> +3V3
- U7 pad 24: unconnected-(U7-VDD-Pad24) -> +3V3
- U7 pad 3: unconnected-(U7-A2-Pad3) -> +3V3
- U7 pad 4: unconnected-(U7-IO0_0-Pad4) -> LED-B08
- U7 pad 5: unconnected-(U7-IO0_1-Pad5) -> LED-B07
- U7 pad 6: unconnected-(U7-IO0_2-Pad6) -> LED-B06
- U7 pad 7: unconnected-(U7-IO0_3-Pad7) -> LED-B05
- U7 pad 8: unconnected-(U7-IO0_4-Pad8) -> LED-B04
- U7 pad 9: unconnected-(U7-IO0_5-Pad9) -> LED-B03
- U8 pad 1: unconnected-(U8-~{INT}-Pad1) -> EXP_INT5
- U8 pad 10: unconnected-(U8-IO0_6-Pad10) -> LED-A09
- U8 pad 11: unconnected-(U8-IO0_7-Pad11) -> LED-A11
- U8 pad 12: unconnected-(U8-VSS-Pad12) -> GND
- U8 pad 13: unconnected-(U8-IO1_0-Pad13) -> LED-A12
- U8 pad 14: unconnected-(U8-IO1_1-Pad14) -> LED-A05
- U8 pad 15: unconnected-(U8-IO1_2-Pad15) -> LED-A03
- U8 pad 16: unconnected-(U8-IO1_3-Pad16) -> LED-A02
- U8 pad 17: unconnected-(U8-IO1_4-Pad17) -> LED-A15
- U8 pad 18: unconnected-(U8-IO1_5-Pad18) -> LED-A16
- U8 pad 19: unconnected-(U8-IO1_6-Pad19) -> LED-E01
- U8 pad 2: unconnected-(U8-A1-Pad2) -> GND
- U8 pad 20: unconnected-(U8-IO1_7-Pad20) -> LED-E02
- U8 pad 21: unconnected-(U8-A0-Pad21) -> GND
- U8 pad 24: unconnected-(U8-VDD-Pad24) -> +3V3
- U8 pad 3: unconnected-(U8-A2-Pad3) -> GND
- U8 pad 4: unconnected-(U8-IO0_0-Pad4) -> LED-A10
- U8 pad 5: unconnected-(U8-IO0_1-Pad5) -> LED-A07
- U8 pad 6: unconnected-(U8-IO0_2-Pad6) -> LED-A04
- U8 pad 7: unconnected-(U8-IO0_3-Pad7) -> LED-A01
- U8 pad 8: unconnected-(U8-IO0_4-Pad8) -> LED-A06
- U8 pad 9: unconnected-(U8-IO0_5-Pad9) -> LED-A08
- U9 pad 1: unconnected-(U9-~{INT}-Pad1) -> EXP_INT6
- U9 pad 10: unconnected-(U9-IO0_6-Pad10) -> Button-A01
- U9 pad 11: unconnected-(U9-IO0_7-Pad11) -> Button-A11
- U9 pad 12: unconnected-(U9-VSS-Pad12) -> GND
- U9 pad 13: unconnected-(U9-IO1_0-Pad13) -> ENC2-X21
- U9 pad 14: unconnected-(U9-IO1_1-Pad14) -> ENC2-X22
- U9 pad 15: unconnected-(U9-IO1_2-Pad15) -> Button-A12
- U9 pad 16: unconnected-(U9-IO1_3-Pad16) -> ENC2-X25
- U9 pad 17: unconnected-(U9-IO1_4-Pad17) -> Button-A05
- U9 pad 18: unconnected-(U9-IO1_5-Pad18) -> ENC2-X23
- U9 pad 19: unconnected-(U9-IO1_6-Pad19) -> Button-A03
- U9 pad 2: unconnected-(U9-A1-Pad2) -> GND
- U9 pad 20: unconnected-(U9-IO1_7-Pad20) -> Button-A02
- U9 pad 21: unconnected-(U9-A0-Pad21) -> +3V3
- U9 pad 24: unconnected-(U9-VDD-Pad24) -> +3V3
- U9 pad 3: unconnected-(U9-A2-Pad3) -> GND
- U9 pad 4: unconnected-(U9-IO0_0-Pad4) -> Button-A10
- U9 pad 5: unconnected-(U9-IO0_1-Pad5) -> Button-A06
- U9 pad 6: unconnected-(U9-IO0_2-Pad6) -> Button-A07
- U9 pad 7: unconnected-(U9-IO0_3-Pad7) -> Button-A08
- U9 pad 8: unconnected-(U9-IO0_4-Pad8) -> Button-A04
- U9 pad 9: unconnected-(U9-IO0_5-Pad9) -> Button-A09
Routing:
- net +3V3: track 0.00 -> 695.4 mm, vias 0 -> 14
- net GND: track 0.00 -> 373.0 mm, vias 0 -> 136
- net VCC: track 0.00 -> 371.8 mm
- net I2C1_SCL: track 0.00 -> 204.5 mm, vias 0 -> 5
- net I2C1_SDA: track 0.00 -> 200.4 mm, vias 0 -> 5
- net EXP_INT4: track 0.00 -> 178.7 mm, vias 0 -> 2
- net EXP_INT3: track 0.00 -> 153.7 mm, vias 0 -> 2
- net EXP_INT8: track 0.00 -> 146.3 mm, vias 0 -> 2
- net AIN1: track 0.00 -> 142.2 mm, vias 0 -> 2
- net AIN2: track 0.00 -> 140.9 mm, vias 0 -> 2
- net I2C2_SCL: track 0.00 -> 135.4 mm, vias 0 -> 5
- net EXP_INT2: track 0.00 -> 134.2 mm, vias 0 -> 2
- net EXP_INT7: track 0.00 -> 121.5 mm, vias 0 -> 2
- net Button-~{D01}: track 0.00 -> 115.5 mm, vias 0 -> 1
- net EXP_INT1: track 0.00 -> 113.4 mm, vias 0 -> 2
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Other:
- outline, holes or cut-outs redrawn
- board text added: "3.3V"
- board text added: "BOOT0"
- board text added: "Debug LED"
- board text added: "GND"
- board text added: "RESET"
- board text added: "RST"
- board text added: "SWCLK"
- board text added: "SWDIO"
